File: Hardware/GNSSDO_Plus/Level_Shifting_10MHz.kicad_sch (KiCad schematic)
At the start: 50 parts, among them J10 SMA_Edge, J8 SMA_Edge, U15 74LVC2T45DC, U16 74LVC2T45DC, U17 LMV7219M5, U20 LMV7219M5

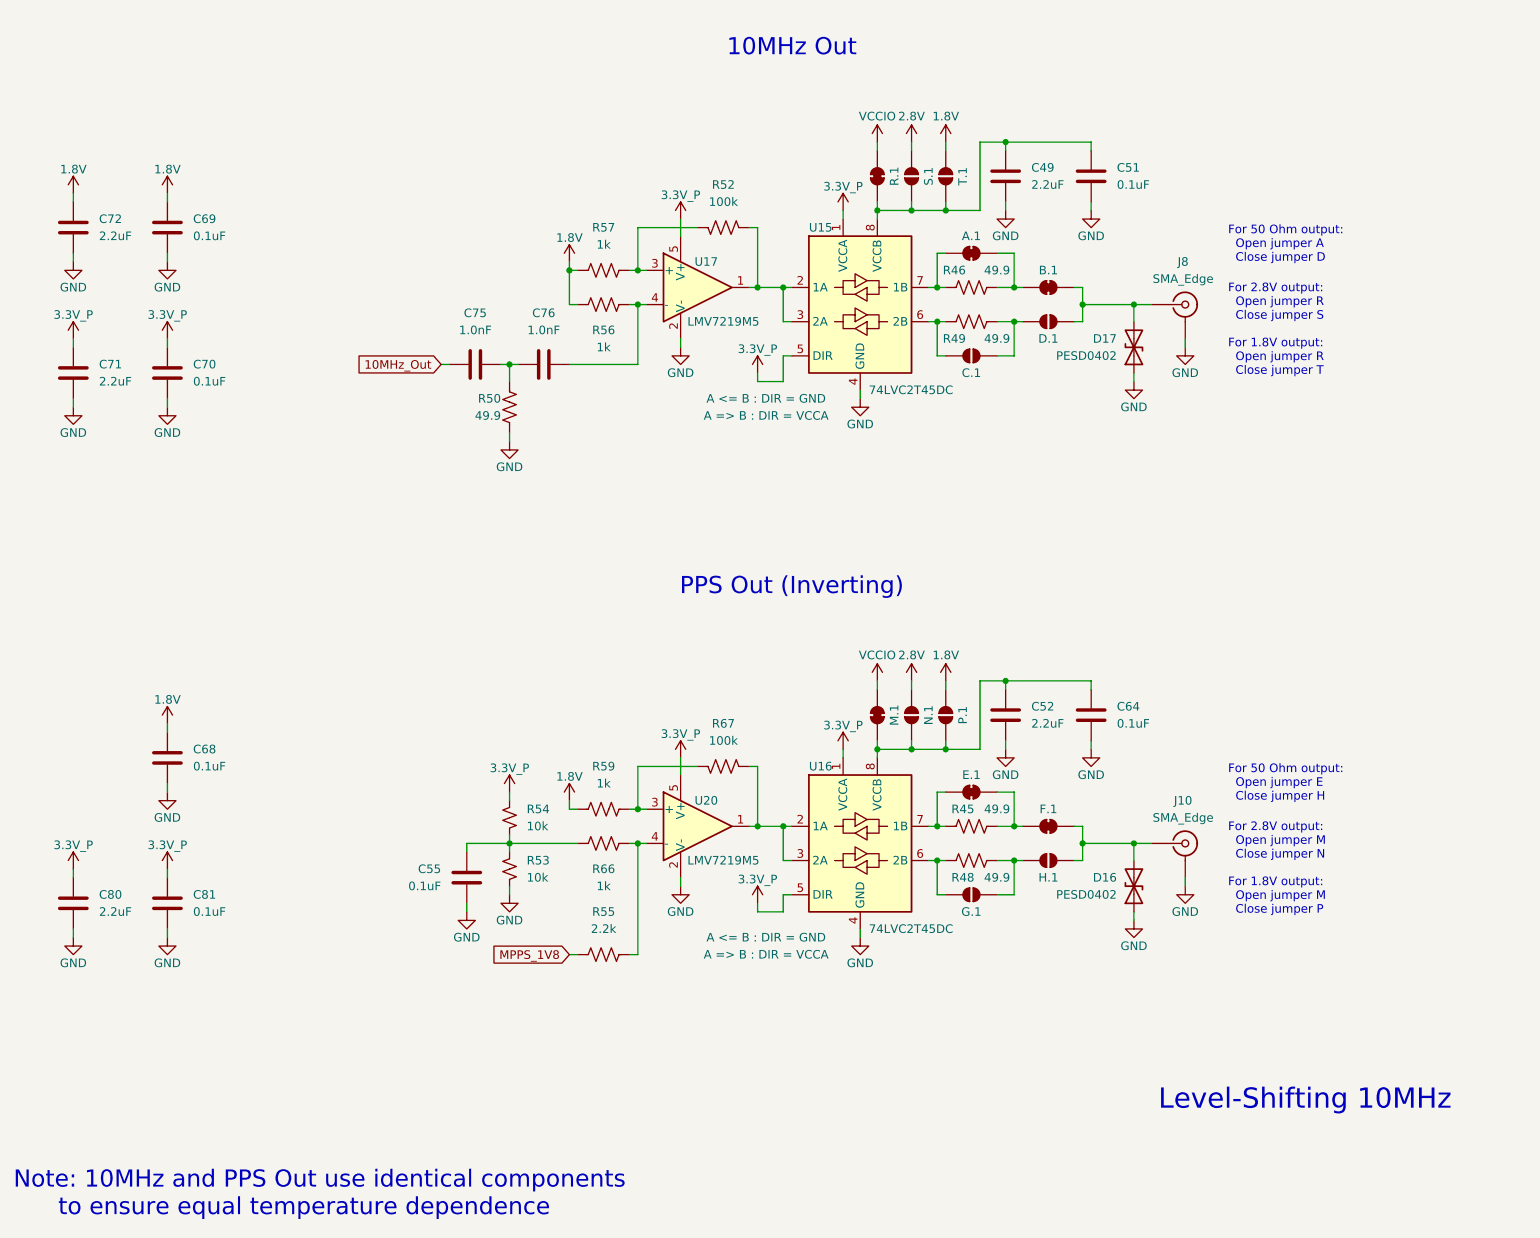
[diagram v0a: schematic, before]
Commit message: GNSSDO Plus: add 3-way splitter
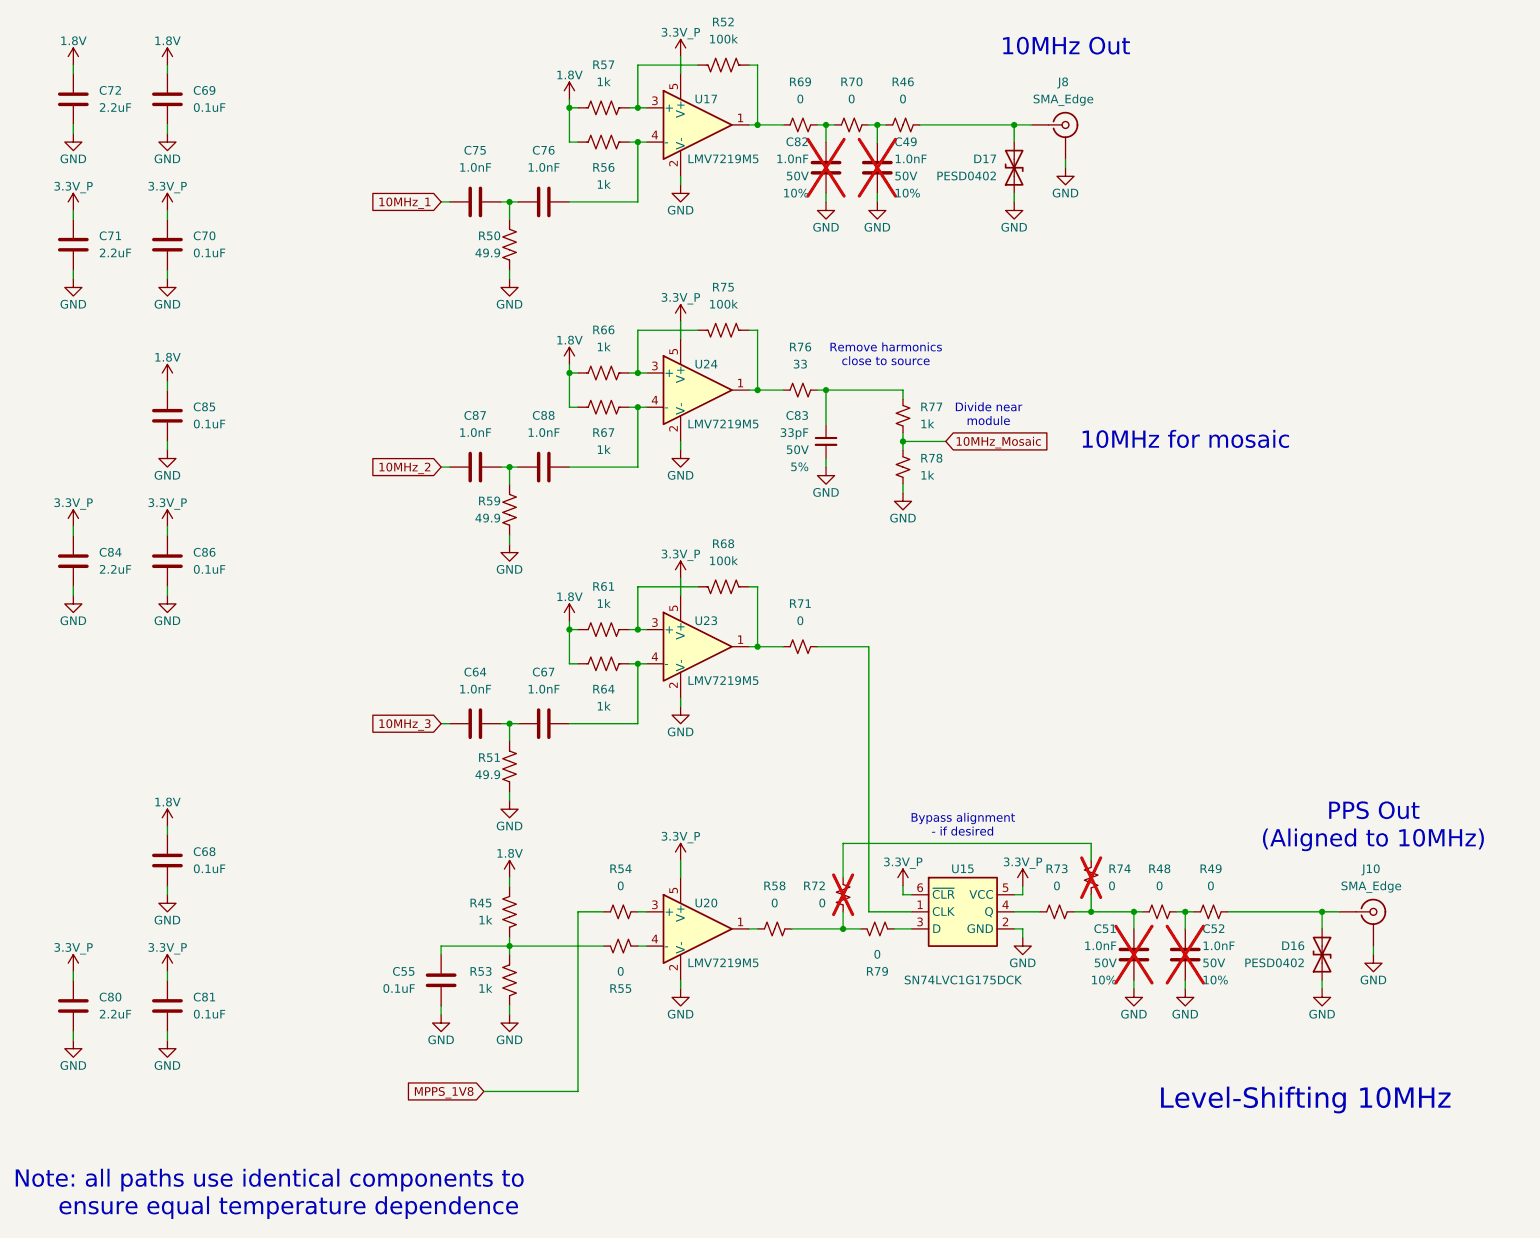
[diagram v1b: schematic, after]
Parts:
- removed A.1, B.1, E.1, F.1, M.1, R.1: ~, SparkFun-Jumper:Jumper_2_NC_Trace, symbol SparkFun-Jumper:SolderJumper_2_Bridged
- removed C.1, D.1, G.1, H.1, N.1, P.1, S.1, T.1: ~, SparkFun-Jumper:Jumper_2_NO, symbol SparkFun-Jumper:SolderJumper_2_Open
- removed C49, C52: 2.2uF, SparkFun-Capacitor:C_0603_1608Metric, symbol SparkFun-Capacitor:2.2uF_0603_10V_20%
- removed C51, C64: 0.1uF, SparkFun-Capacitor:C_0603_1608Metric, symbol SparkFun-Capacitor:0.1uF_0603_25V_20%
- removed R45, R46, R48, R49: 49.9, SparkFun-Resistor:R_0603_1608Metric, symbol SparkFun-Resistor:49.9_0603
- removed R53, R54: 10k, SparkFun-Resistor:R_0603_1608Metric, symbol SparkFun-Resistor:10k_0603
- removed R55: 2.2k, SparkFun-Resistor:R_0603_1608Metric, symbol SparkFun-Resistor:2.2k_0603
- removed R59: 1k, SparkFun-Resistor:R_0603_1608Metric, symbol SparkFun-Resistor:1k_0603
- removed R67: 100k, SparkFun-Resistor:R_0603_1608Metric, symbol SparkFun-Resistor:100k_0603
- removed U15, U16: 74LVC2T45DC, SparkFun-Semiconductor-Standard:VSSOP8_SOT765-1, symbol SparkFun-IC-Logic:74LVC2T45DC
- added C49, C51, C52, C64, C67, C82, C87, C88: 1.0nF, SparkFun-Capacitor:C_0603_1608Metric, symbol SparkFun-Capacitor:1.0nF_0603_50V_10%
- added C83: 33pF, SparkFun-Capacitor:C_0603_1608Metric, symbol SparkFun-Capacitor:33pF_0603_50V_5%
- added C84: 2.2uF, SparkFun-Capacitor:C_0603_1608Metric, symbol SparkFun-Capacitor:2.2uF_0603_10V_20%
- added C85, C86: 0.1uF, SparkFun-Capacitor:C_0603_1608Metric, symbol SparkFun-Capacitor:0.1uF_0603_25V_20%
- added R45, R53, R61, R64, R67, R77, R78: 1k, SparkFun-Resistor:R_0603_1608Metric, symbol SparkFun-Resistor:1k_0603
- added R46, R48, R49, R54, R55, R58, R69, R70, R71, R72, R73, R74, R79: 0, SparkFun-Resistor:R_0603_1608Metric, symbol SparkFun-Resistor:0_0603
- added R51, R59: 49.9, SparkFun-Resistor:R_0603_1608Metric, symbol SparkFun-Resistor:49.9_0603
- added R68, R75: 100k, SparkFun-Resistor:R_0603_1608Metric, symbol SparkFun-Resistor:100k_0603
- added R76: 33, SparkFun-Resistor:R_0603_1608Metric, symbol SparkFun-Resistor:33_0603
- added U15: SN74LVC1G175DCK, SparkFun-Semiconductor-Standard:SOT-323, symbol SparkFun-IC-Logic:74LVC1G175
- added U23, U24: LMV7219M5, SparkFun-Semiconductor-Standard:SOT23-5, symbol SparkFun-IC-Amplifier:LMV7219M5
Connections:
- net 1.8V: now also R66.1, C85.1, R45.2, R61.1, R64.1, R67.1
- net 3.3V_P: now also C84.1, C86.1, U15.5 (VCC), U15.6 (~{CLR}), U23.5 (V+), U24.5 (V+)
- net GND: now also C49.2, C51.2, C52.2, C82.2, C83.2, C84.2, C85.2, C86.2, R51.1, R53.1, R59.1, R78.2, U15.2 (GND), U23.2 (V-), U24.2 (V-)
- net MPPS_1V8: now also R54.1
- net at D16.2 (A2), J10.1 (In): now also R49.2
- net at U20.1: now also R58.1
- net at U20.3 (+): now also R54.2
- net at U20.4 (-): now also R55.2; no longer R66.2
- net at C55.1: now also R45.1, R53.2, R55.1; no longer R66.1
- net at D17.2 (A2), J8.1 (In): now also R46.2
- net at R52.1, U17.1: now also R69.1
- net 10MHz_Out renamed 10MHz_1
- new net: C49.1, R46.1, R70.2
- new net: R58.2, R72.1, R79.1
- new net: R72.2, R74.2
- new net: C51.1, R48.1, R73.2, R74.1
- new net: C82.1, R69.2, R70.1
- new net: C52.1, R48.2, R49.1
- new net: R79.2, U15.3 (D)
- new net: C64.2, C67.1, R51.2
- new net: C83.1, R76.2, R77.1
- new net: C87.2, C88.1, R59.2
- new net: C88.2, R67.2, U24.4 (-)
- new net: R66.2, R75.2, U24.3 (+)
- new net: R71.2, U15.1 (CLK)
- new net: R73.1, U15.4 (Q)
- new net: R75.1, R76.1, U24.1
- new net: R68.1, R71.1, U23.1
- new net: R61.2, R68.2, U23.3 (+)
- new net: C67.2, R64.2, U23.4 (-)
- new net 10MHz_2: C87.1
- new net 10MHz_3: C64.1
- new net 10MHz_Mosaic: R77.2, R78.1
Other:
- note added: "10MHz for mosaic"
- note added: "Bypass alignment - if desired"
- note added: "Divide near module"
- note added: "Note: all paths use identical components to ensure equal temperature dependence"
- note added: "PPS Out (Aligned to 10MHz)"
- note added: "Remove harmonics close to source"
- note removed: "For 2.8V output: Open jumper M Close jumper N For 1.8V output: Open jumper M Close jumper P"
- note removed: "For 2.8V output: Open jumper R Close jumper S For 1.8V output: Open jumper R Close jumper T"
- note removed: "For 50 Ohm output: Open jumper A Close jumper D"
- note removed: "For 50 Ohm output: Open jumper E Close jumper H"
- note removed: "Note: 10MHz and PPS Out use identical components to ensure equal temperature dependence"
- note removed: "PPS Out (Inverting)"
- moved on the sheet: C55, C68, C69, C70, C71, C72, C75, C76, C80, C81, D16, D17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

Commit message: GNSSDO+ WIP
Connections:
- net 3.3V_P renamed 3.3V_A

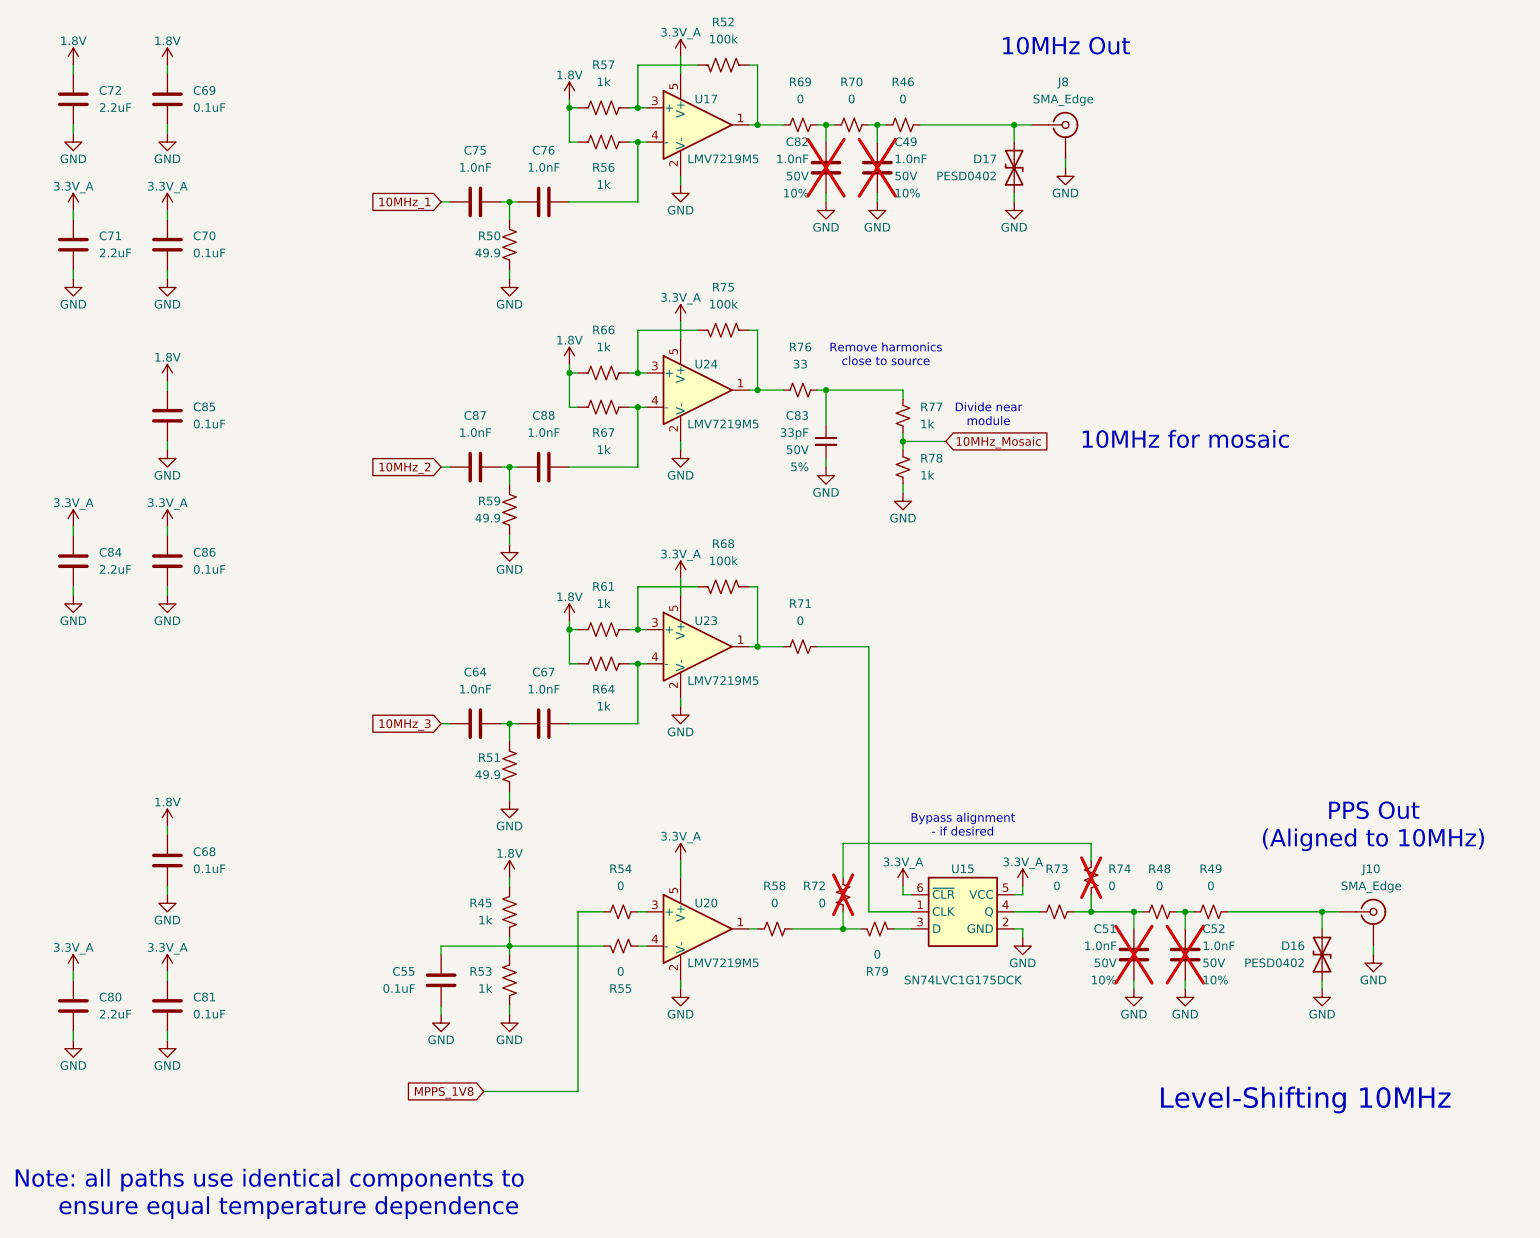
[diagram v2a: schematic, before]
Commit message: GNSSDO+ routed
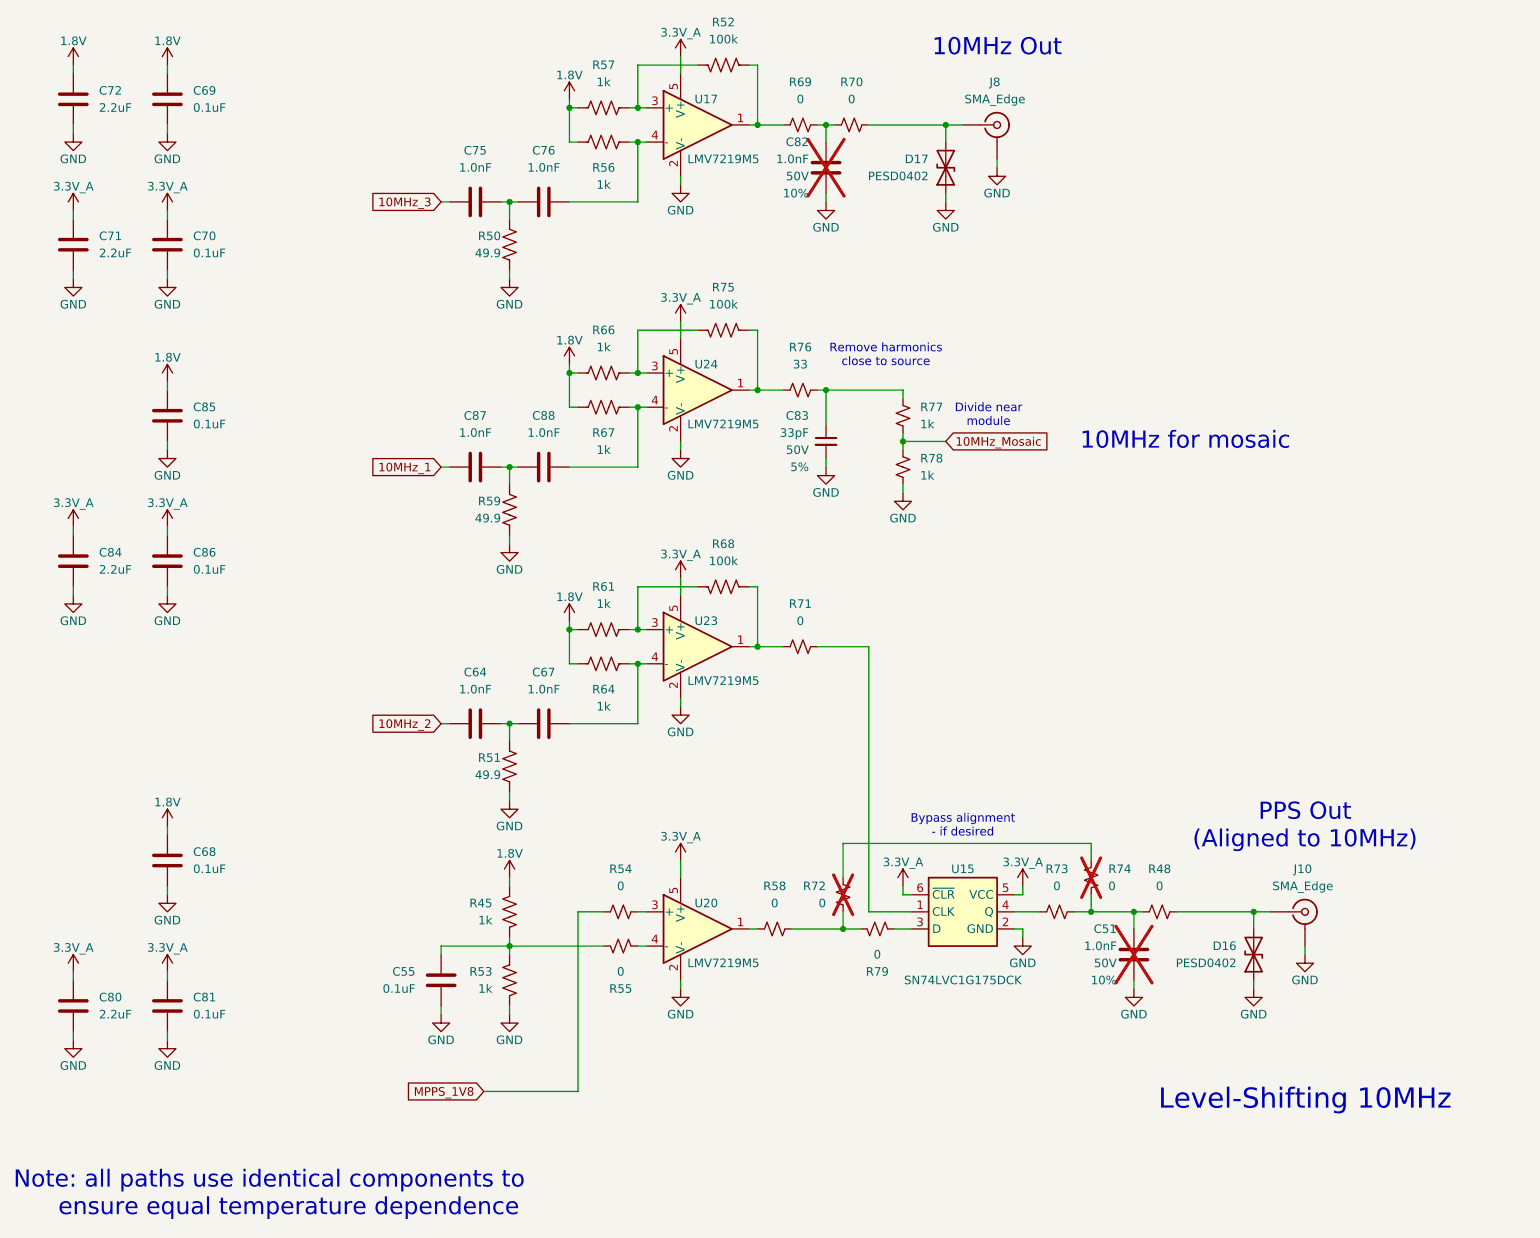
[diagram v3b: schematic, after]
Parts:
- removed C49, C52: 1.0nF, SparkFun-Capacitor:C_0603_1608Metric, symbol SparkFun-Capacitor:1.0nF_0603_50V_10%
- removed R46, R49: 0, SparkFun-Resistor:R_0603_1608Metric, symbol SparkFun-Resistor:0_0603
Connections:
- net 10MHz_1: now also C87.1; no longer C75.1
- net 10MHz_2: now also C64.1; no longer C87.1
- net 10MHz_3: now also C75.1; no longer C64.1
- net at D16.2 (A2), J10.1 (In): now also R48.2
- net at R70.2: now also D17.2 (A2), J8.1 (In)
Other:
- moved on the sheet: D16, D17, J10, J8
